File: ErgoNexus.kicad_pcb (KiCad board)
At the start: 2 copper layers, 174.3 x 138 mm, 110 parts, among them J7 Conn_01x02, J8 Conn_01x02, SW1 SW_Push, SW2 RotaryEncoder_Switch, SW3 SW_Push, SW4 RotaryEncoder_Switch, U1 SuperMini nRF52840, U2 SuperMini nRF52840

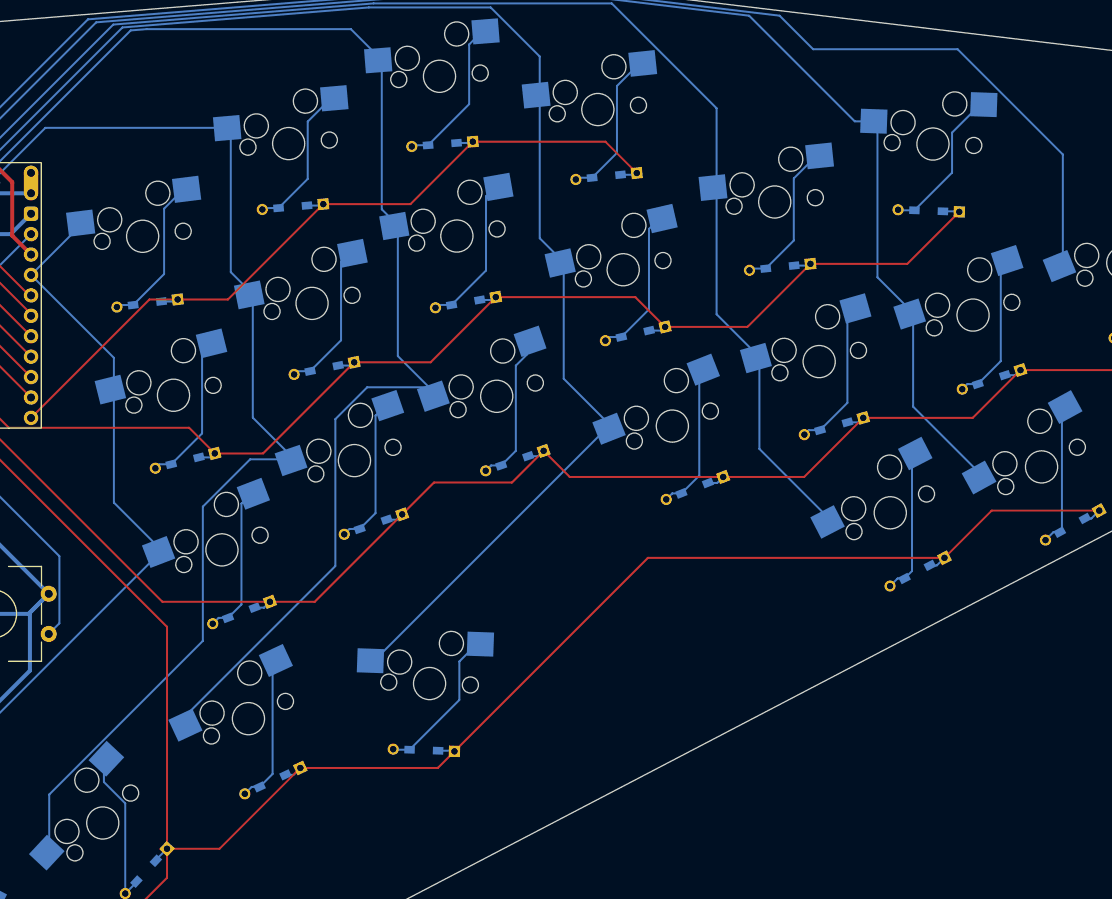
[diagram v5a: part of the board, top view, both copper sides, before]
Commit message: feat: add screw hole
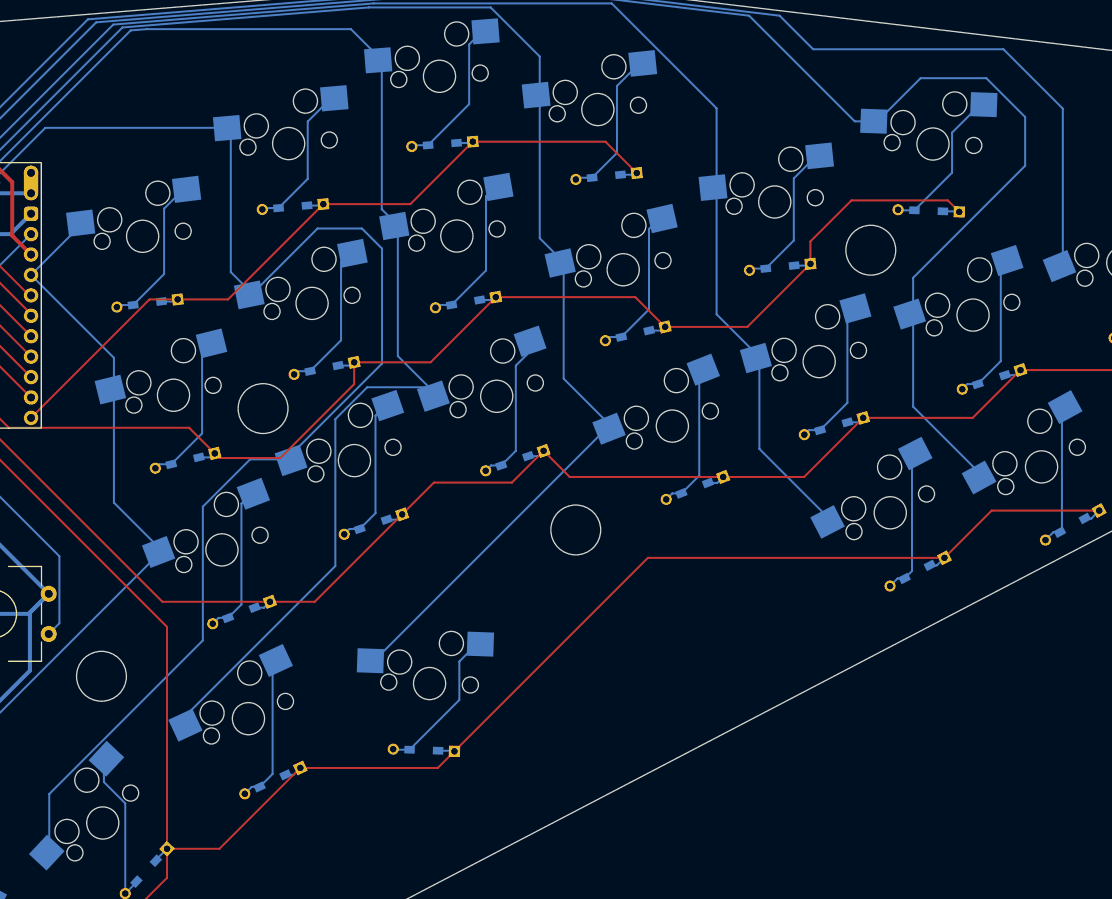
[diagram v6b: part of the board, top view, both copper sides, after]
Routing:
- net Col2_R: track 156.9 -> 185.5 mm
- net Col6_R: track 206.5 -> 233.6 mm
- net Row2_R: track 151.9 -> 156.8 mm
- net Col7_R: track 200.1 -> 203.5 mm
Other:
- outline, holes or cut-outs redrawn
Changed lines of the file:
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@@
 		(at 229.085 139.679666 90)
 		(property "Reference" "R4"
-			(at -0.2 -1.6 -90)
+			(at -0.2 -1.6 270)
 			(layer "B.SilkS")
 			(effects
@@
 		(layer "Dwgs.User")
 	)
+	(gr_circle
+		(center 315.885 130.179666)
+		(end 318.985 130.179666)
+		(stroke
+			(width 0.05)
+			(type default)
+		)
+		(fill yes)
+		(layer "Edge.Cuts")
+	)
+	(gr_circle
+		(center 276.985 115.079666)
+		(end 280.085 115.079666)
+		(stroke
+			(width 0.05)
+			(type default)
+		)
+		(fill yes)
+		(layer "Edge.Cuts")
+	)
 	(gr_poly
 		(pts
@@
 		(layer "Edge.Cuts")
 	)
+	(gr_circle
+		(center 352.585 95.379666)
+		(end 355.685 95.379666)
+		(stroke
+			(width 0.05)
+			(type default)
+		)
+		(fill yes)
+		(layer "Edge.Cuts")
+	)
+	(gr_circle
+		(center 256.885 148.379666)
+		(end 259.985 148.379666)
+		(stroke
+			(width 0.05)
+			(type default)
+		)
+		(fill yes)
+		(layer "Edge.Cuts")
+	)
+	(gr_circle
+		(center 276.985 115.079666)
+		(end 281.985 115.079666)
+		(stroke
+			(width 0.1)
+			(type default)
+		)
+		(fill no)
+		(layer "Margin")
+	)
+	(gr_circle
+		(center 256.885 148.379666)
+		(end 261.885 148.379666)
+		(stroke
+			(width 0.1)
+			(type default)
+		)
+		(fill no)
+		(layer "Margin")
+	)
+	(gr_circle
+		(center 352.585 95.379666)
+		(end 357.585 95.379666)
+		(stroke
+			(width 0.1)
+			(type default)
+		)
+		(fill no)
+		(layer "Margin")
+	)
+	(gr_circle
+		(center 315.885 130.179666)
+		(end 320.885 130.179666)
+		(stroke
+			(width 0.1)
+			(type default)
+		)
+		(fill no)
+		(layer "Margin")
+	)
 	(segment
 		(start 236.685 130.079666)
@@
 	)
 	(segment
+		(start 271.558044 121.234161)
+		(end 270.981827 120.657944)
+		(width 0.25)
+		(layer "F.Cu")
+		(net 37)
+	)
+	(segment
 		(start 305.93712 101.218066)
 		(end 323.292814 101.218066)
@@
 	)
 	(segment
+		(start 363.592679 90.612633)
+		(end 362.159712 89.179666)
+		(width 0.25)
+		(layer "F.Cu")
+		(net 37)
+	)
+	(segment
+		(start 345.074128 94.290538)
+		(end 345.074128 97.081413)
+		(width 0.25)
+		(layer "F.Cu")
+		(net 37)
+	)
+	(segment
 		(start 326.99735 104.922602)
 		(end 337.232939 104.922602)
@@
 	)
 	(segment
+		(start 288.319833 112.044833)
+		(end 279.130505 121.234161)
+		(width 0.25)
+		(layer "F.Cu")
+		(net 37)
+	)
+	(segment
 		(start 267.789549 117.465666)
 		(end 270.981827 120.657944)
@@
 	)
 	(segment
-		(start 345.074128 97.081413)
-		(end 357.123899 97.081413)
+		(start 362.159712 89.179666)
+		(end 350.185 89.179666)
 		(width 0.25)
 		(layer "F.Cu")
@@
 	)
 	(segment
-		(start 276.988481 120.657944)
-		(end 288.319833 109.326592)
+		(start 288.319833 109.326592)
+		(end 288.319833 112.044833)
 		(width 0.25)
 		(layer "F.Cu")
@@
 	)
 	(segment
-		(start 323.292814 101.218066)
-		(end 326.99735 104.922602)
+		(start 350.185 89.179666)
+		(end 345.074128 94.290538)
 		(width 0.25)
 		(layer "F.Cu")
@@
 	)
 	(segment
-		(start 357.123899 97.081413)
-		(end 363.592679 90.612633)
+		(start 323.292814 101.218066)
+		(end 326.99735 104.922602)
 		(width 0.25)
 		(layer "F.Cu")
@@
 	)
 	(segment
-		(start 270.981827 120.657944)
-		(end 276.988481 120.657944)
+		(start 279.130505 121.234161)
+		(end 271.558044 121.234161)
 		(width 0.25)
 		(layer "F.Cu")
@@
 	)
 	(segment
-		(start 275.711303 100.84768)
-		(end 275.711303 116.208519)
+		(start 291.785 95.179666)
+		(end 291.785 109.479666)
 		(width 0.25)
 		(layer "B.Cu")
@@
 	)
 	(segment
-		(start 250.386897 163.088464)
-		(end 250.386897 169.9899)
+		(start 291.785 109.479666)
+		(end 280.894429 120.370237)
 		(width 0.25)
 		(layer "B.Cu")
@@
 	)
 	(segment
-		(start 280.894429 121.391645)
-		(end 275.381974 121.391645)
+		(start 289.285 92.679666)
+		(end 291.785 95.179666)
+		(width 0.25)
+		(layer "B.Cu")
+		(net 76)
+	)
+	(segment
+		(start 275.381974 121.391645)
+		(end 269.495544 127.278075)
 		(width 0.25)
 		(layer "B.Cu")
@@
 	)
 	(segment
-		(start 275.381974 121.391645)
-		(end 269.495544 127.278075)
+		(start 250.386897 163.033116)
+		(end 250.386897 169.9899)
 		(width 0.25)
 		(layer "B.Cu")
@@
 	)
 	(segment
-		(start 275.711303 116.208519)
-		(end 280.894429 121.391645)
+		(start 275.711303 100.73827)
+		(end 283.769907 92.679666)
+		(width 0.25)
+		(layer "B.Cu")
+		(net 76)
+	)
+	(segment
+		(start 275.711303 100.84768)
+		(end 275.711303 100.73827)
 		(width 0.25)
 		(layer "B.Cu")
@@
 	)
 	(segment
+		(start 269.495544 143.924469)
+		(end 250.386897 163.033116)
+		(width 0.25)
+		(layer "B.Cu")
+		(net 76)
+	)
+	(segment
+		(start 283.769907 92.679666)
+		(end 289.285 92.679666)
+		(width 0.25)
+		(layer "B.Cu")
+		(net 76)
+	)
+	(segment
+		(start 280.894429 121.391645)
+		(end 275.381974 121.391645)
+		(width 0.25)
+		(layer "B.Cu")
+		(net 76)
+	)
+	(segment
 		(start 269.495544 127.278075)
-		(end 269.495544 143.979817)
+		(end 269.495544 143.924469)
 		(width 0.25)
 		(layer "B.Cu")
@@
 	)
 	(segment
-		(start 272.969852 98.106229)
-		(end 275.711303 100.84768)
+		(start 280.894429 120.370237)
+		(end 280.894429 121.391645)
 		(width 0.25)
 		(layer "B.Cu")
@@
 	)
 	(segment
-		(start 269.495544 143.979817)
-		(end 250.386897 163.088464)
+		(start 272.969852 98.106229)
+		(end 275.711303 100.84768)
 		(width 0.25)
 		(layer "B.Cu")
@@
 	)
 	(segment
+		(start 371.785 84.879666)
+		(end 357.849343 98.815323)
+		(width 0.25)
+		(layer "B.Cu")
+		(net 82)
+	)
+	(segment
 		(start 319.688799 64.079666)
 		(end 337.44859 66.206316)
@@
 	)
 	(segment
+		(start 358.782369 73.979666)
+		(end 366.958349 73.979666)
+		(width 0.25)
+		(layer "B.Cu")
+		(net 82)
+	)
+	(segment
+		(start 353.41334 79.348695)
+		(end 358.782369 73.979666)
+		(width 0.25)
+		(layer "B.Cu")
+		(net 82)
+	)
+	(segment
 		(start 240.285 87.079666)
 		(end 240.285 82.979666)
@@
 	)
 	(segment
+		(start 371.785 78.806317)
+		(end 371.785 84.879666)
+		(width 0.25)
+		(layer "B.Cu")
+		(net 82)
+	)
+	(segment
 		(start 337.44859 66.206316)
 		(end 350.590969 79.348695)
@@
 	)
 	(segment
-		(start 353.41334 79.348695)
-		(end 353.41334 98.748264)
+		(start 366.958349 73.979666)
+		(end 371.785 78.806317)
+		(width 0.25)
+		(layer "B.Cu")
+		(net 82)
+	)
+	(segment
+		(start 357.849343 98.815323)
+		(end 357.849343 103.184267)
 		(width 0.25)
 		(layer "B.Cu")
@@
 	)
 	(segment
-		(start 353.41334 98.748264)
-		(end 357.849343 103.184267)
-		(width 0.25)
-		(layer "B.Cu")
-		(net 82)
-	)
-	(segment
 		(start 292.544156 64.079666)
 		(end 319.688799 64.079666)
@@
 	)
 	(segment
-		(start 317.63629 63.379666)
-		(end 341.241827 66.206316)
+		(start 255.200418 66.664248)
+		(end 295.587545 63.379666)
 		(width 0.25)
 		(layer "B.Cu")
@@
 	)
 	(segment
-		(start 363.385 70.379666)
-		(end 376.473133 83.467799)
+		(start 238.785 86.279666)
+		(end 238.785 83.079666)
 		(width 0.25)
 		(layer "B.Cu")
@@
 	)
 	(segment
-		(start 345.415177 70.379666)
-		(end 363.385 70.379666)
+		(start 341.241827 66.206316)
+		(end 345.415177 70.379666)
 		(width 0.25)
 		(layer "B.Cu")
@@
 	)
 	(segment
-		(start 295.587545 63.379666)
-		(end 317.63629 63.379666)
+		(start 238.785 83.079666)
+		(end 255.200418 66.664248)
 		(width 0.25)
 		(layer "B.Cu")
@@
 	)
 	(segment
-		(start 376.473133 83.467799)
-		(end 376.473133 97.188222)
+		(start 345.415177 70.379666)
+		(end 369.085 70.379666)
 		(width 0.25)
 		(layer "B.Cu")
@@
 	)
 	(segment
-		(start 341.241827 66.206316)
-		(end 345.415177 70.379666)
+		(start 295.587545 63.379666)
+		(end 317.63629 63.379666)
 		(width 0.25)
 		(layer "B.Cu")
@@
 	)
 	(segment
-		(start 255.200418 66.664248)
-		(end 295.587545 63.379666)
+		(start 317.63629 63.379666)
+		(end 341.241827 66.206316)
 		(width 0.25)
 		(layer "B.Cu")
@@
 	)
 	(segment
-		(start 238.785 83.079666)
-		(end 255.200418 66.664248)
+		(start 369.085 70.379666)
+		(end 376.473133 77.767799)
 		(width 0.25)
 		(layer "B.Cu")
@@
 	)
 	(segment
-		(start 238.785 86.279666)
-		(end 238.785 83.079666)
+		(start 376.473133 77.767799)
+		(end 376.473133 97.188222)
 		(width 0.25)
 		(layer "B.Cu")
@@
 		(members "3e335188-7622-4f30-a0a4-b498c25e4a12" "5b5f851f-2580-490f-b441-229322c46bfc")
 	)
+	(group ""
+		(members "2cfbd696-6369-43f0-a901-0a9b1f2e4e11" "e51323da-51c0-4bc9-b365-2258d7a53d75")
+	)
+	(group ""
+		(members "3638d80d-f0b1-449d-a62c-064a4863fe73" "c736ab5f-1cc7-4362-b144-3622b1b22382")
+	)
+	(group ""
+		(members "0b8333e4-44a8-4e09-ad00-3e472eebb89a" "35417649-d02c-4f8c-9422-d2d3b001a80b")
+	)
+	(group ""
+		(members "257cf81c-003e-48fa-ba11-256b38860cbe" "e85bd4d2-2c20-421e-8011-27d05bd86674")
+	)
 	(embedded_fonts no)

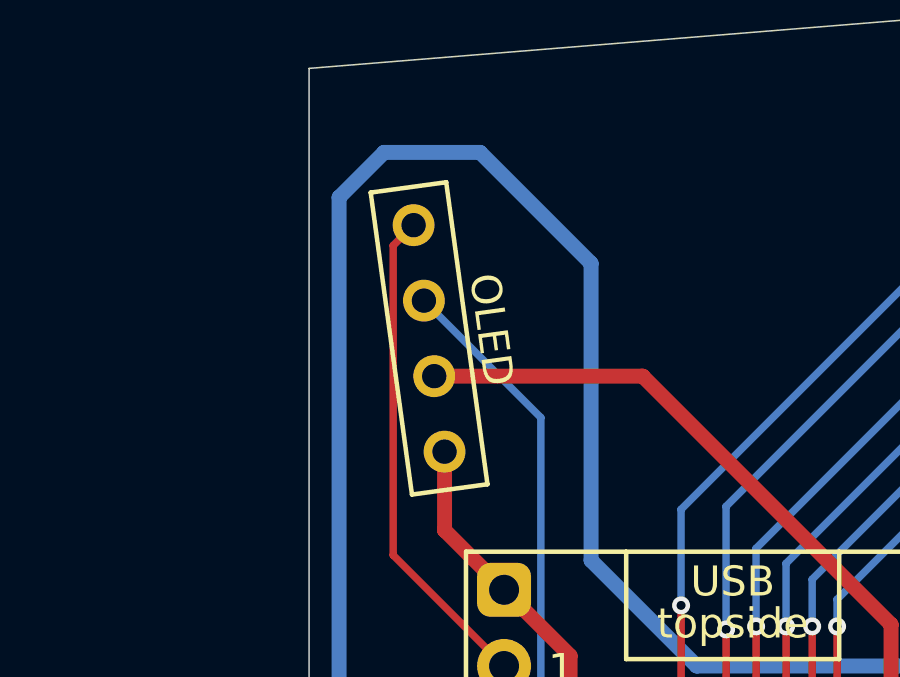
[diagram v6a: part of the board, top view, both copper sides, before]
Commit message: fix: fix oled angle
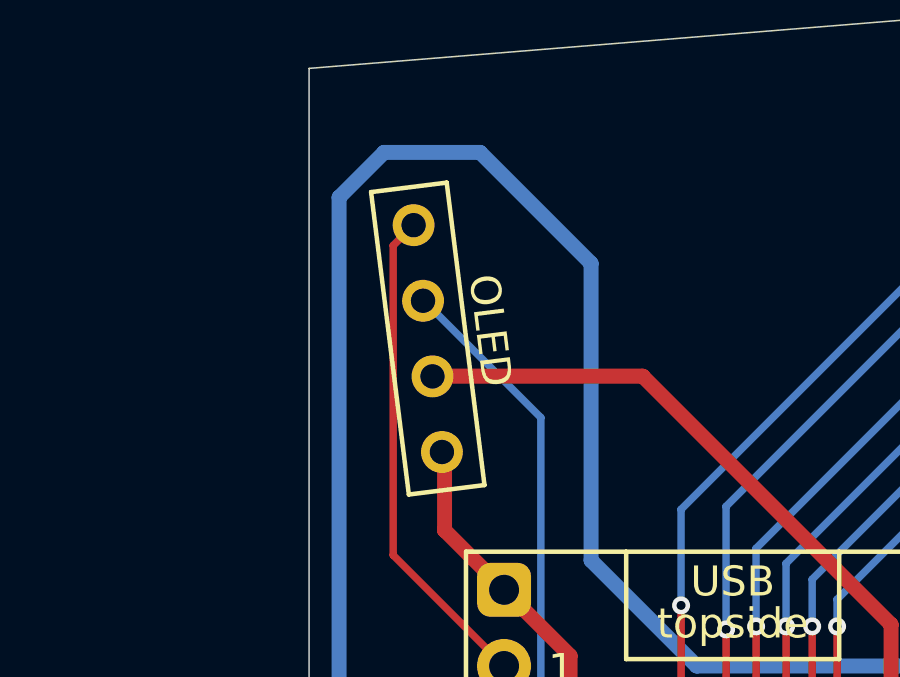
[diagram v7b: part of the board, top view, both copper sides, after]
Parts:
- turned OL8 to -82.88 degrees
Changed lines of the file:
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@@
 	(footprint "kbd_Parts:OLED"
 		(layer "F.Cu")
-		(at 229.869242 73.604737 -82.22)
+		(at 229.869242 73.604737 -82.88)
 		(descr "Connecteur 6 pins")
 		(tags "CONN DEV")
 		(property "Reference" "OL8"
-			(at 3.699999 2.1 97.78)
+			(at 3.699999 2.1 97.12)
 			(layer "F.Fab")
 			(effects
@@
 		)
 		(property "Value" "OLED"
-			(at 3.6 3.3 97.78)
+			(at 3.600001 3.300001 97.12)
 			(layer "F.SilkS")
 			(hide yes)
@@
 		)
 		(property "Datasheet" ""
-			(at 0 0 97.78)
+			(at 0 0 97.12)
 			(layer "F.Fab")
 			(hide yes)
@@
 		)
 		(property "Description" ""
-			(at 0 0 97.78)
+			(at 0 0 97.12)
 			(layer "F.Fab")
 			(hide yes)
@@
 		(fp_line
 			(start -1.27 1.270001)
-			(end 8.89 1.27)
+			(end 8.889999 1.27)
 			(stroke
 				(width 0.15)
@@
 		(fp_line
 			(start 8.890001 -1.27)
-			(end 8.89 1.27)
+			(end 8.889999 1.27)
 			(stroke
 				(width 0.15)
@@
 		)
 		(fp_text user "OLED"
-			(at 3.800001 -2.1 97.78)
+			(at 3.800001 -2.1 97.12)
 			(layer "F.SilkS")
 			(effects
@@
 		)
 		(pad "1" thru_hole circle
-			(at 0 0 277.78)
+			(at 0 0 277.12)
 			(size 1.397 1.397)
 			(drill 0.8128)
@@
 		)
 		(pad "2" thru_hole circle
-			(at 2.54 0 277.78)
+			(at 2.540001 0.000001 277.12)
 			(size 1.397 1.397)
 			(drill 0.8128)
@@
 		)
 		(pad "3" thru_hole circle
-			(at 5.080001 0 277.78)
+			(at 5.08 0 277.12)
 			(size 1.397 1.397)
 			(drill 0.8128)
@@
 		)
 		(pad "4" thru_hole circle
-			(at 7.620001 0 277.78)
+			(at 7.620001 0.000001 277.12)
 			(size 1.397 1.397)
 			(drill 0.8128)
